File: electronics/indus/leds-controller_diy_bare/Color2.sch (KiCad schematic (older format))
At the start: 14 parts

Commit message: wip bare diy controller - dcdc and refactor
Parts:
- gave numbers to parts that had none: 14
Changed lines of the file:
@@
 $Descr A4 11693 8268
 encoding utf-8
-Sheet 3 8
+Sheet 3 9
 Title "Carte controlleur de LEDs 4 canaux"
 Date ""
@@
 VIN_24V
 $Comp
-L TPS92513 U?
+L TPS92513 U3
 U 1 1 57157FFA
 P 5850 3300
-F 0 "U?" H 6200 2350 60  0000 C CNN
+F 0 "U3" H 6200 2350 60  0000 C CNN
 F 1 "TPS92513" H 5450 2350 60  0000 C CNN
 F 2 "" H 6000 3400 60  0000 C CNN
@@
 	1150 3200 5300 3200
 $Comp
-L GND-RESCUE-leds-controller #PWR?
+L GND-RESCUE-leds-controller #PWR017
 U 1 1 57158002
 P 3400 2850
-F 0 "#PWR?" H 3400 2850 30  0001 C CNN
+F 0 "#PWR017" H 3400 2850 30  0001 C CNN
 F 1 "GND" H 3400 2780 30  0001 C CNN
 F 2 "" H 3400 2850 60  0000 C CNN
@@
 $EndComp
 $Comp
-L C-RESCUE-leds-controller C?
+L C-RESCUE-leds-controller C11
 U 1 1 57158008
 P 3400 2400
-F 0 "C?" H 3400 2500 40  0000 L CNN
+F 0 "C11" H 3400 2500 40  0000 L CNN
 F 1 "C" H 3406 2315 40  0000 L CNN
 F 2 "" H 3438 2250 30  0000 C CNN
@@
 $EndComp
 $Comp
-L R-RESCUE-leds-controller R?
+L R-RESCUE-leds-controller R12
 U 1 1 5715800F
 P 4150 2450
-F 0 "R?" V 4230 2450 40  0000 C CNN
+F 0 "R12" V 4230 2450 40  0000 C CNN
 F 1 "R" V 4157 2451 40  0000 C CNN
 F 2 "" V 4080 2450 30  0000 C CNN
@@
 Connection ~ 4150 3200
 $Comp
-L C-RESCUE-leds-controller C?
+L C-RESCUE-leds-controller C9
 U 1 1 57158019
 P 1650 3900
-F 0 "C?" H 1650 4000 40  0000 L CNN
+F 0 "C9" H 1650 4000 40  0000 L CNN
 F 1 "C" H 1656 3815 40  0000 L CNN
 F 2 "" H 1688 3750 30  0000 C CNN
@@
 Connection ~ 5800 4650
 $Comp
-L GND-RESCUE-leds-controller #PWR?
+L GND-RESCUE-leds-controller #PWR018
 U 1 1 57158027
 P 6000 5000
-F 0 "#PWR?" H 6000 5000 30  0001 C CNN
+F 0 "#PWR018" H 6000 5000 30  0001 C CNN
 F 1 "GND" H 6000 4930 30  0001 C CNN
 F 2 "" H 6000 5000 60  0000 C CNN
@@
 Connection ~ 6000 4650
 $Comp
-L R-RESCUE-leds-controller R?
+L R-RESCUE-leds-controller R9
 U 1 1 5715802E
 P 2200 3550
-F 0 "R?" V 2280 3550 40  0000 C CNN
+F 0 "R9" V 2280 3550 40  0000 C CNN
 F 1 "R" V 2207 3551 40  0000 C CNN
 F 2 "" V 2130 3550 30  0000 C CNN
@@
 $EndComp
 $Comp
-L R-RESCUE-leds-controller R?
+L R-RESCUE-leds-controller R10
 U 1 1 57158035
 P 2200 4250
-F 0 "R?" V 2280 4250 40  0000 C CNN
+F 0 "R10" V 2280 4250 40  0000 C CNN
 F 1 "R" V 2207 4251 40  0000 C CNN
 F 2 "" V 2130 4250 30  0000 C CNN
@@
 Connection ~ 2200 3900
 $Comp
-L C-RESCUE-leds-controller C?
+L C-RESCUE-leds-controller C10
 U 1 1 57158045
 P 3100 4050
-F 0 "C?" H 3100 4150 40  0000 L CNN
+F 0 "C10" H 3100 4150 40  0000 L CNN
 F 1 "C" H 3106 3965 40  0000 L CNN
 F 2 "" H 3138 3900 30  0000 C CNN
@@
 $EndComp
 $Comp
-L R-RESCUE-leds-controller R?
+L R-RESCUE-leds-controller R11
 U 1 1 5715804C
 P 4100 4250
-F 0 "R?" V 4180 4250 40  0000 C CNN
+F 0 "R11" V 4180 4250 40  0000 C CNN
 F 1 "R" V 4107 4251 40  0000 C CNN
 F 2 "" V 4030 4250 30  0000 C CNN
@@
 Connection ~ 4100 4650
 $Comp
-L INDUCTOR L?
+L INDUCTOR L2
 U 1 1 5715805B
 P 8250 3200
-F 0 "L?" V 8200 3200 40  0000 C CNN
+F 0 "L2" V 8200 3200 40  0000 C CNN
 F 1 "XAL6060-153MEC - 15µH - 6A" V 8350 3200 40  0000 C CNN
 F 2 "risebox:SELF_COILCRAFT_XAL6060-153" H 8250 3200 60  0001 C CNN
@@
 	6050 2700 6050 2000
 $Comp
-L C-RESCUE-leds-controller C?
+L C-RESCUE-leds-controller C12
 U 1 1 5715806B
 P 6850 2650
-F 0 "C?" H 6850 2750 40  0000 L CNN
+F 0 "C12" H 6850 2750 40  0000 L CNN
 F 1 "C" H 6856 2565 40  0000 L CNN
 F 2 "" H 6888 2500 30  0000 C CNN
@@
 	8550 3200 10500 3200
 $Comp
-L C-RESCUE-leds-controller C?
+L C-RESCUE-leds-controller C13
 U 1 1 5715807C
 P 9600 3500
-F 0 "C?" H 9600 3600 40  0000 L CNN
+F 0 "C13" H 9600 3600 40  0000 L CNN
 F 1 "C" H 9606 3415 40  0000 L CNN
 F 2 "" H 9638 3350 30  0000 C CNN
@@
 Connection ~ 9600 3800
 $Comp
-L R-RESCUE-leds-controller R?
+L R-RESCUE-leds-controller R13
 U 1 1 57158087
 P 8250 3800
-F 0 "R?" V 8330 3800 40  0000 C CNN
+F 0 "R13" V 8330 3800 40  0000 C CNN
 F 1 "R" V 8257 3801 40  0000 C CNN
 F 2 "" V 8180 3800 30  0000 C CNN
@@
 	8500 3800 10500 3800
 $Comp
-L R-RESCUE-leds-controller R?
+L R-RESCUE-leds-controller R14
 U 1 1 57158090
 P 10200 4250
-F 0 "R?" V 10280 4250 40  0000 C CNN
+F 0 "R14" V 10280 4250 40  0000 C CNN
 F 1 "R" V 10207 4251 40  0000 C CNN
 F 2 "" V 10130 4250 30  0000 C CNN
@@
 	10200 4650 10200 4500
 $Comp
-L DIODESCH D?
+L DIODESCH D3
 U 1 1 5715809A
 P 7400 4250
-F 0 "D?" H 7400 4350 40  0000 C CNN
+F 0 "D3" H 7400 4350 40  0000 C CNN
 F 1 "DIODESCH" H 7400 4150 40  0000 C CNN
 F 2 "" H 7400 4250 60  0000 C CNN

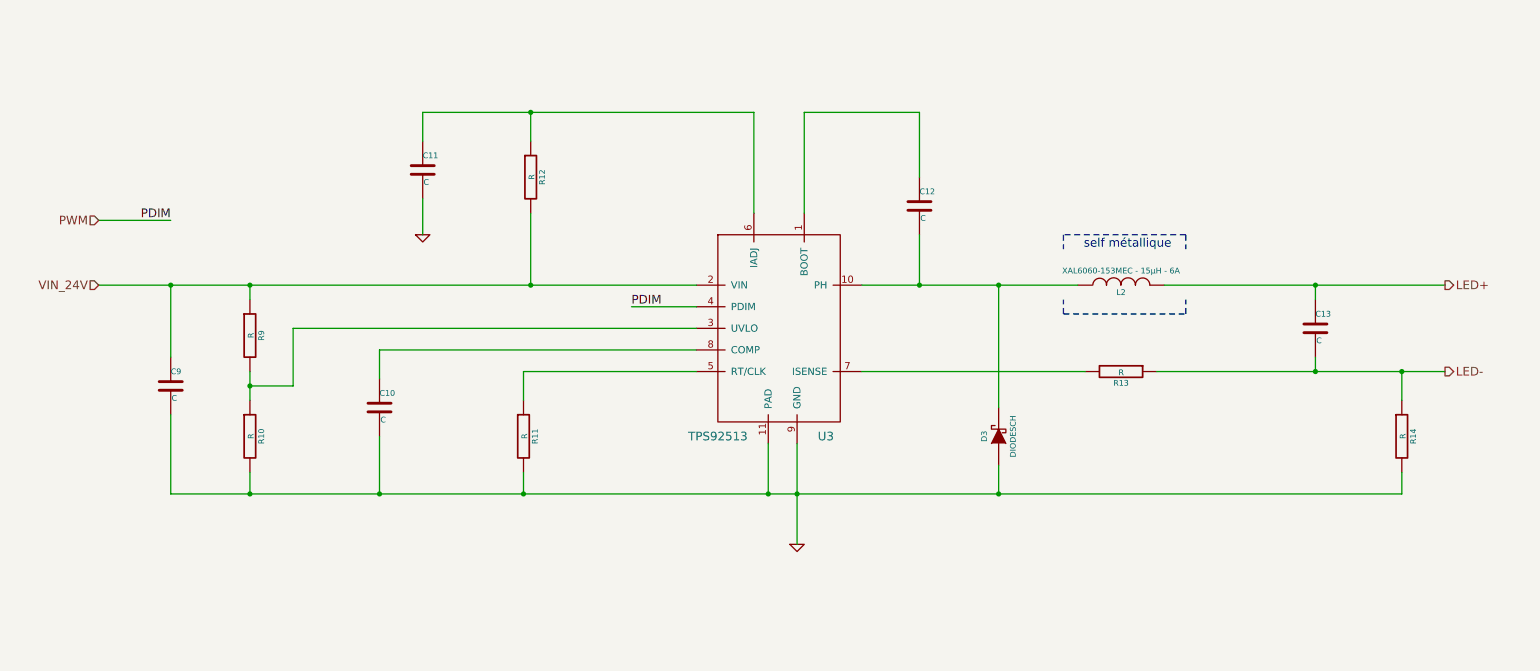
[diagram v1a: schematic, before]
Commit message: schema done - misses values
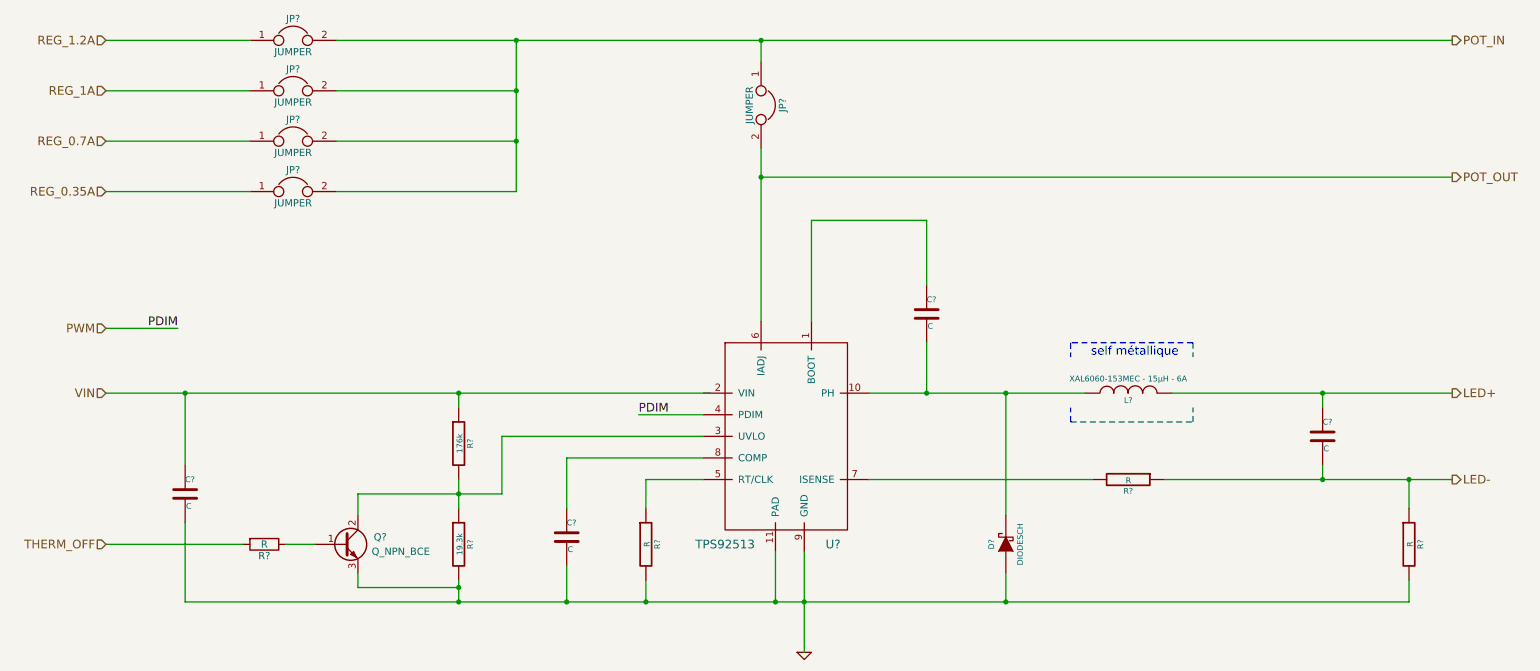
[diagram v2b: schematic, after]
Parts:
- removed C10, C11, C12, C13, C9: C, symbol C-RESCUE-leds-controller
- removed D3: DIODESCH, symbol DIODESCH
- removed L2: XAL6060-153MEC - 15µH - 6A, risebox:SELF_COILCRAFT_XAL6060-153, symbol INDUCTOR
- removed R10, R11, R12, R13, R14, R9: R, symbol R-RESCUE-leds-controller
- removed U3: TPS92513, symbol TPS92513
- added C? (x4): C, symbol C-RESCUE-leds-controller
- added D?: DIODESCH, symbol DIODESCH
- added JP? (x5): JUMPER, symbol JUMPER
- added L?: XAL6060-153MEC - 15µH - 6A, risebox:SELF_COILCRAFT_XAL6060-153, symbol INDUCTOR
- added Q?: Q_NPN_BCE, symbol Q_NPN_BCE
- added R?: 176k, symbol R-RESCUE-leds-controller
- added R?: 19.3k, symbol R-RESCUE-leds-controller
- added R? (x3): R, symbol R-RESCUE-leds-controller
- added R?: R, symbol R
- added U?: TPS92513, symbol TPS92513
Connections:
- net GND: now also C?.2, C?.2, D?.1 (A), Q?.3 (E), R?.2, R?.2, R?.2, U?.11 (PAD), U?.9 (GND)
- net LED+: now also C?.1, L?.2
- net LED-: now also C?.2, R?.1, R?.1
- net PWM: now also U?.4 (PDIM)
- new net: C?.1, U?.1 (BOOT)
- new net: C?.2, D?.2 (K), L?.1, U?.10 (PH)
- new net: Q?.2 (C), R?.1, R?.2, U?.3 (UVLO)
- new net: R?.1, U?.5 (RT/CLK)
- new net: R?.2, U?.7 (ISENSE)
- new net: C?.1, U?.8 (COMP)
- new net: Q?.1 (B), R?.1
- new net POT_IN: JP?.1, JP?.2, JP?.2, JP?.2, JP?.2
- new net POT_OUT: JP?.2, U?.6 (IADJ)
- new net REG_0.35A: JP?.1
- new net REG_0.7A: JP?.1
- new net REG_1.2A: JP?.1
- new net REG_1A: JP?.1
- new net THERM_OFF: R?.2
- new net VIN: C?.1, R?.1

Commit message: schema prctically ok missing refs
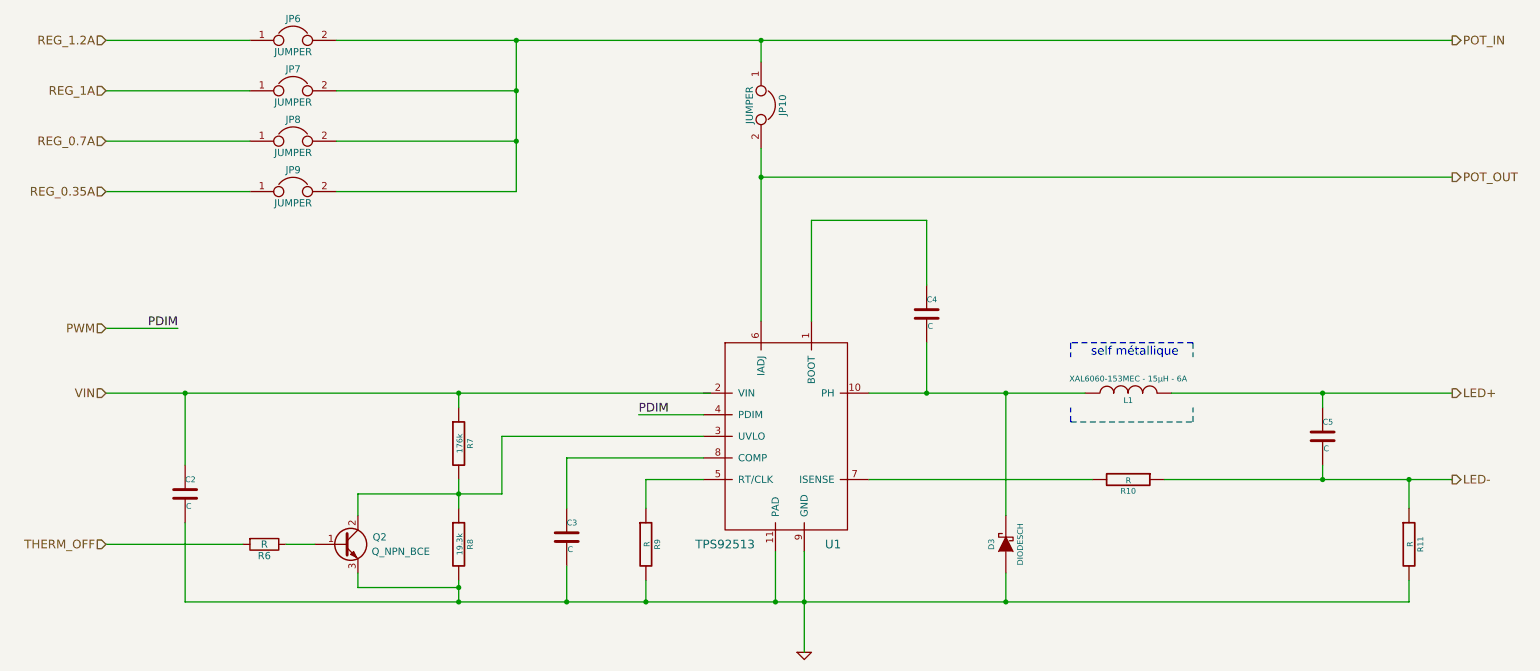
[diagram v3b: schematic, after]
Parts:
- gave numbers to parts that had none: 19
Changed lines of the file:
@@
 VIN
 $Comp
-L TPS92513 U?
+L TPS92513 U1
 U 1 1 5766268C
 P 5900 4050
-F 0 "U?" H 6250 3100 60  0000 C CNN
+F 0 "U1" H 6250 3100 60  0000 C CNN
 F 1 "TPS92513" H 5500 3100 60  0000 C CNN
 F 2 "" H 6050 4150 60  0000 C CNN
@@
 $EndComp
 $Comp
-L C-RESCUE-leds-controller C?
+L C-RESCUE-leds-controller C2
 U 1 1 57662693
 P 1750 4650
-F 0 "C?" H 1750 4750 40  0000 L CNN
+F 0 "C2" H 1750 4750 40  0000 L CNN
 F 1 "C" H 1756 4565 40  0000 L CNN
 F 2 "" H 1788 4500 30  0000 C CNN
@@
 $EndComp
 $Comp
-L GND-RESCUE-leds-controller #PWR?
+L GND-RESCUE-leds-controller #PWR11
 U 1 1 5766269A
 P 6050 5750
-F 0 "#PWR?" H 6050 5750 30  0001 C CNN
+F 0 "#PWR11" H 6050 5750 30  0001 C CNN
 F 1 "GND" H 6050 5680 30  0001 C CNN
 F 2 "" H 6050 5750 60  0000 C CNN
@@
 $EndComp
 $Comp
-L R-RESCUE-leds-controller R?
+L R-RESCUE-leds-controller R7
 U 1 1 576626A0
 P 3650 4300
-F 0 "R?" V 3730 4300 40  0000 C CNN
+F 0 "R7" V 3730 4300 40  0000 C CNN
 F 1 "176k" V 3657 4301 40  0000 C CNN
 F 2 "" V 3580 4300 30  0000 C CNN
@@
 $EndComp
 $Comp
-L R-RESCUE-leds-controller R?
+L R-RESCUE-leds-controller R8
 U 1 1 576626A7
 P 3650 5000
-F 0 "R?" V 3730 5000 40  0000 C CNN
+F 0 "R8" V 3730 5000 40  0000 C CNN
 F 1 "19.3k" V 3657 5001 40  0000 C CNN
 F 2 "" V 3580 5000 30  0000 C CNN
@@
 $EndComp
 $Comp
-L C-RESCUE-leds-controller C?
+L C-RESCUE-leds-controller C3
 U 1 1 576626AE
 P 4400 4950
-F 0 "C?" H 4400 5050 40  0000 L CNN
+F 0 "C3" H 4400 5050 40  0000 L CNN
 F 1 "C" H 4406 4865 40  0000 L CNN
 F 2 "" H 4438 4800 30  0000 C CNN
@@
 $EndComp
 $Comp
-L R-RESCUE-leds-controller R?
+L R-RESCUE-leds-controller R9
 U 1 1 576626B5
 P 4950 5000
-F 0 "R?" V 5030 5000 40  0000 C CNN
+F 0 "R9" V 5030 5000 40  0000 C CNN
 F 1 "R" V 4957 5001 40  0000 C CNN
 F 2 "" V 4880 5000 30  0000 C CNN
@@
 $EndComp
 $Comp
-L INDUCTOR L?
+L INDUCTOR L1
 U 1 1 576626BC
 P 8300 3950
-F 0 "L?" V 8250 3950 40  0000 C CNN
+F 0 "L1" V 8250 3950 40  0000 C CNN
 F 1 "XAL6060-153MEC - 15µH - 6A" V 8400 3950 40  0000 C CNN
 F 2 "risebox:SELF_COILCRAFT_XAL6060-153" H 8300 3950 60  0001 C CNN
@@
 self métallique
 $Comp
-L C-RESCUE-leds-controller C?
+L C-RESCUE-leds-controller C4
 U 1 1 576626C4
 P 6900 3400
-F 0 "C?" H 6900 3500 40  0000 L CNN
+F 0 "C4" H 6900 3500 40  0000 L CNN
 F 1 "C" H 6906 3315 40  0000 L CNN
 F 2 "" H 6938 3250 30  0000 C CNN
@@
 $EndComp
 $Comp
-L C-RESCUE-leds-controller C?
+L C-RESCUE-leds-controller C5
 U 1 1 576626CB
 P 9650 4250
-F 0 "C?" H 9650 4350 40  0000 L CNN
+F 0 "C5" H 9650 4350 40  0000 L CNN
 F 1 "C" H 9656 4165 40  0000 L CNN
 F 2 "" H 9688 4100 30  0000 C CNN
@@
 $EndComp
 $Comp
-L R-RESCUE-leds-controller R?
+L R-RESCUE-leds-controller R10
 U 1 1 576626D2
 P 8300 4550
-F 0 "R?" V 8380 4550 40  0000 C CNN
+F 0 "R10" V 8380 4550 40  0000 C CNN
 F 1 "R" V 8307 4551 40  0000 C CNN
 F 2 "" V 8230 4550 30  0000 C CNN
@@
 $EndComp
 $Comp
-L R-RESCUE-leds-controller R?
+L R-RESCUE-leds-controller R11
 U 1 1 576626D9
 P 10250 5000
-F 0 "R?" V 10330 5000 40  0000 C CNN
+F 0 "R11" V 10330 5000 40  0000 C CNN
 F 1 "R" V 10257 5001 40  0000 C CNN
 F 2 "" V 10180 5000 30  0000 C CNN
@@
 $EndComp
 $Comp
-L DIODESCH D?
+L DIODESCH D3
 U 1 1 576626E0
 P 7450 5000
-F 0 "D?" H 7450 5100 40  0000 C CNN
+F 0 "D3" H 7450 5100 40  0000 C CNN
 F 1 "DIODESCH" H 7450 4900 40  0000 C CNN
 F 2 "" H 7450 5000 60  0000 C CNN
@@
 PDIM
 $Comp
-L JUMPER JP?
+L JUMPER JP6
 U 1 1 576626EA
 P 2500 1500
-F 0 "JP?" H 2500 1650 50  0000 C CNN
+F 0 "JP6" H 2500 1650 50  0000 C CNN
 F 1 "JUMPER" H 2500 1420 50  0000 C CNN
 F 2 "" H 2500 1500 50  0000 C CNN
@@
 $EndComp
 $Comp
-L JUMPER JP?
+L JUMPER JP7
 U 1 1 576626F1
 P 2500 1850
-F 0 "JP?" H 2500 2000 50  0000 C CNN
+F 0 "JP7" H 2500 2000 50  0000 C CNN
 F 1 "JUMPER" H 2500 1770 50  0000 C CNN
 F 2 "" H 2500 1850 50  0000 C CNN
@@
 $EndComp
 $Comp
-L JUMPER JP?
+L JUMPER JP8
 U 1 1 576626F8
 P 2500 2200
-F 0 "JP?" H 2500 2350 50  0000 C CNN
+F 0 "JP8" H 2500 2350 50  0000 C CNN
 F 1 "JUMPER" H 2500 2120 50  0000 C CNN
 F 2 "" H 2500 2200 50  0000 C CNN
@@
 $EndComp
 $Comp
-L JUMPER JP?
+L JUMPER JP9
 U 1 1 576626FF
 P 2500 2550
-F 0 "JP?" H 2500 2700 50  0000 C CNN
+F 0 "JP9" H 2500 2700 50  0000 C CNN
 F 1 "JUMPER" H 2500 2470 50  0000 C CNN
 F 2 "" H 2500 2550 50  0000 C CNN
@@
 REG_0.35A
 $Comp
-L JUMPER JP?
+L JUMPER JP10
 U 1 1 5766270A
 P 5750 1950
-F 0 "JP?" H 5750 2100 50  0000 C CNN
+F 0 "JP10" H 5750 2100 50  0000 C CNN
 F 1 "JUMPER" H 5750 1870 50  0000 C CNN
 F 2 "" H 5750 1950 50  0000 C CNN
@@
 Connection ~ 3650 5300
 $Comp
-L Q_NPN_BCE Q?
+L Q_NPN_BCE Q2
 U 1 1 57662775
 P 2850 5000
-F 0 "Q?" H 3150 5050 50  0000 R CNN
+F 0 "Q2" H 3150 5050 50  0000 R CNN
 F 1 "Q_NPN_BCE" H 3450 4950 50  0000 R CNN
 F 2 "" H 3050 5100 50  0000 C CNN
@@
 THERM_OFF
 $Comp
-L R R?
+L R R6
 U 1 1 5766277D
 P 2300 5000
-F 0 "R?" V 2380 5000 50  0000 C CNN
+F 0 "R6" V 2380 5000 50  0000 C CNN
 F 1 "R" V 2300 5000 50  0000 C CNN
 F 2 "" V 2230 5000 50  0000 C CNN
